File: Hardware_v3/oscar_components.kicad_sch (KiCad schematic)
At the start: 71 parts, among them J1 SWD_Header, J10 MIDI_THROUGH, J11 USB_C_Receptacle, J12 Debug_Header, J2 Eurorack_10_pin_power, J3 ChannelC_In, J4 ChannelA_In, J5 ChannelB_In, J6 ChC_Buff_Out, J7 ChA_Buff_Out, J8 ChB_Buff_Out, J9 MIDI_IN, SW1 Reset_Button, SW2 Menu_Button, SW3 Left_Encoder, SW4 Right_Encoder, U1 LT1117-3.3, U2 ILI9341_SPI_Daughterboard, U3 STM32F446RETx, U4 TL074, U5 MCP6004, U6 H11L1, Y1 8MHz

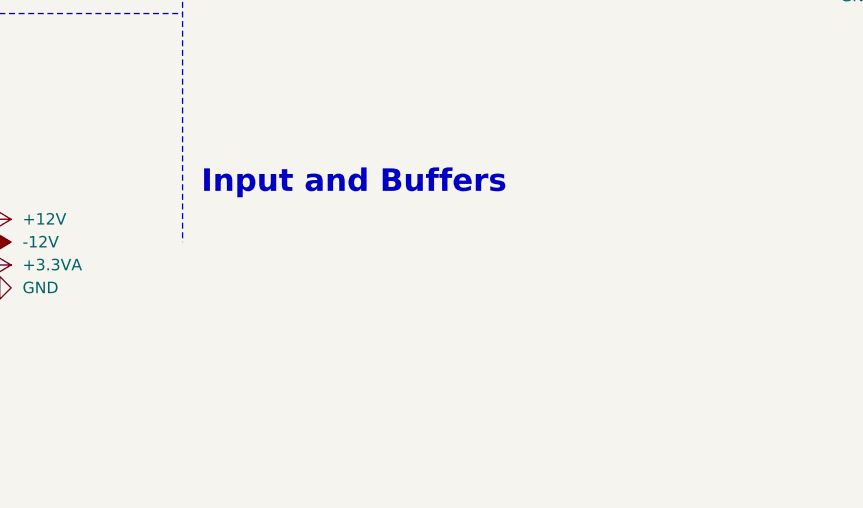
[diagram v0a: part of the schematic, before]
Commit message: Increased size of regulator heat sink vias
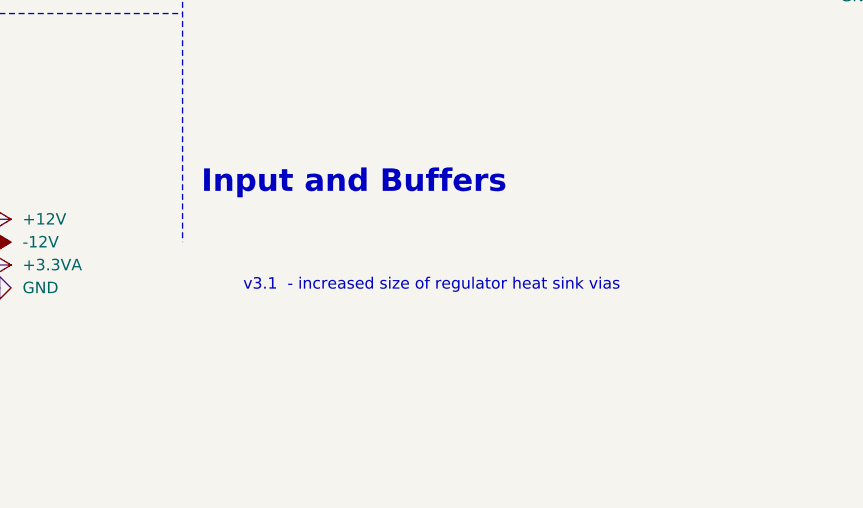
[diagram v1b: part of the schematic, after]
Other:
- note added: "v3.1 - increased size of regulator heat sink vias"
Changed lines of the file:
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@@
 		(title "Oscar")
 		(date "2025-04-03")
-		(rev "v3")
+		(rev "v3.1")
 		(company "Mountjoy Modular")
 	)
@@
 		(effects
 			(font
+				(size 1.27 1.27)
+			)
+		)
+	)
+	(text "v3.1  - increased size of regulator heat sink vias"
+		(exclude_from_sim no)
+		(at 327.406 257.556 0)
+		(effects
+			(font
